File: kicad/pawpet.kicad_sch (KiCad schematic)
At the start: 35 parts, among them J1 USB4105-GF-A, J2 Conn_ARM_JTAG_SWD_10, J3 MOLEX, Q1 DMG2301L, U1 ATSAMD21G18A-A, U3 MX25R1635FM1IL0, Y1 32,768

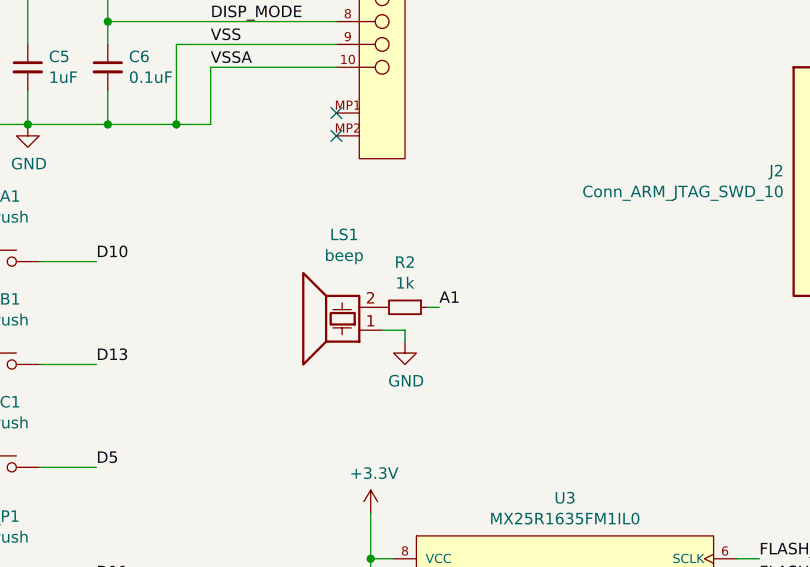
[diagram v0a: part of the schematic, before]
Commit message: updated to use latest adafruit samd base and gclk output to display vcom
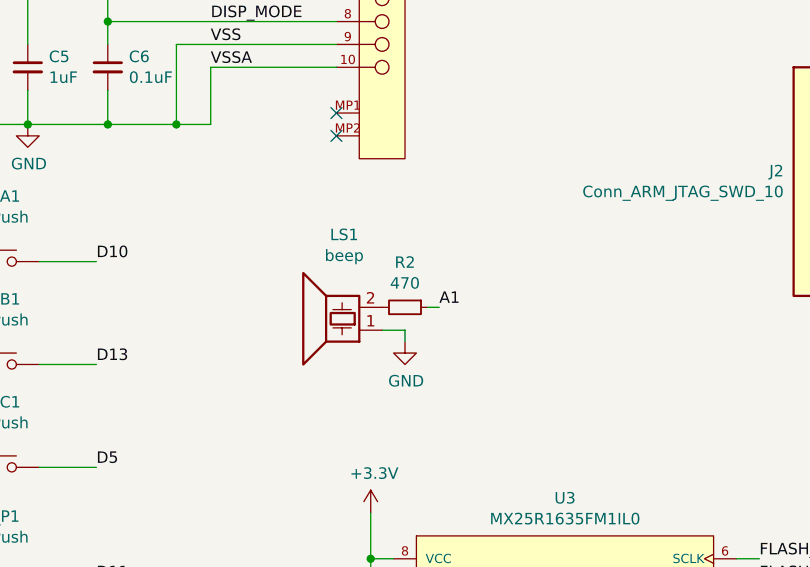
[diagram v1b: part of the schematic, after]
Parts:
- J2: footprint pawpet:ARM_JTAG -> Connector:Tag-Connect_TC2030-IDC-NL_2x03_P1.27mm_Vertical
- R2: value 1k -> 470
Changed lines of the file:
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@@
     (in_bom yes) (on_board yes)
     (property "Reference" "R2" (id 0) (at 87.63 115.6716 90))
-    (property "Value" "1k" (id 1) (at 87.63 117.983 90))
+    (property "Value" "470" (id 1) (at 87.63 117.983 90))
     (property "Footprint" "Resistor_SMD:R_0805_2012Metric" (id 2) (at 87.63 120.65 0)
       (effects (font (size 1.27 1.27)) hide)
@@
       (effects (font (size 1.27 1.27)) (justify right))
     )
-    (property "Footprint" "pawpet:ARM_JTAG" (id 2) (at 140.97 106.68 0)
+    (property "Footprint" "Connector:Tag-Connect_TC2030-IDC-NL_2x03_P1.27mm_Vertical" (id 2) (at 140.97 106.68 0)
       (effects (font (size 1.27 1.27)) hide)
     )
@@
     )
     (path "/00000000-0000-0000-0000-00005f61e5f9"
-      (reference "J2") (unit 1) (value "Conn_ARM_JTAG_SWD_10") (footprint "pawpet:ARM_JTAG")
+      (reference "J2") (unit 1) (value "Conn_ARM_JTAG_SWD_10") (footprint "Connector:Tag-Connect_TC2030-IDC-NL_2x03_P1.27mm_Vertical")
     )
     (path "/00000000-0000-0000-0000-00005f37490d"
@@
     )
     (path "/00000000-0000-0000-0000-00005f60ffb8"
-      (reference "R2") (unit 1) (value "1k") (footprint "Resistor_SMD:R_0805_2012Metric")
+      (reference "R2") (unit 1) (value "470") (footprint "Resistor_SMD:R_0805_2012Metric")
     )
     (path "/00000000-0000-0000-0000-00005f9e88e7"

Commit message: update to latest schematic, pcb, and stl files
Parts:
- J3: footprint pawpet:Molex-52892-1033-Manufacturer_Recommended_handsolder -> molex:Molex-52892-1033-Manufacturer_Recommended
- U1: footprint pawpet:TQFP-48-1EP_7x7mm_P0.5mm_EP5x5mm_handsolder -> Package_QFP:TQFP-48-1EP_7x7mm_P0.5mm_EP5x5mm
- U3: footprint pawpet:Macronix-SOP-8-150MIL-0-0-MFG_handsolder -> Package_SO:SOIC-8_5.23x5.23mm_P1.27mm
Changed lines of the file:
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@@
     (property "Reference" "U1" (id 0) (at 226.06 152.1206 0))
     (property "Value" "ATSAMD21G18A-A" (id 1) (at 226.06 154.432 0))
-    (property "Footprint" "pawpet:TQFP-48-1EP_7x7mm_P0.5mm_EP5x5mm_handsolder" (id 2) (at 248.92 148.59 0)
+    (property "Footprint" "Package_QFP:TQFP-48-1EP_7x7mm_P0.5mm_EP5x5mm" (id 2) (at 248.92 148.59 0)
       (effects (font (size 1.27 1.27)) hide)
     )
@@
       (effects (font (size 1.27 1.27)) hide)
     )
-    (property "Footprint" "pawpet:Molex-52892-1033-Manufacturer_Recommended_handsolder" (id 2) (at 77.47 71.12 0)
+    (property "Footprint" "molex:Molex-52892-1033-Manufacturer_Recommended" (id 2) (at 77.47 71.12 0)
       (effects (font (size 1.27 1.27)) hide)
     )
@@
     (property "Reference" "U3" (id 0) (at 105.41 141.859 0))
     (property "Value" "MX25R1635FM1IL0" (id 1) (at 105.41 144.1704 0))
-    (property "Footprint" "pawpet:Macronix-SOP-8-150MIL-0-0-MFG_handsolder" (id 2) (at 83.82 163.83 0)
+    (property "Footprint" "Package_SO:SOIC-8_5.23x5.23mm_P1.27mm" (id 2) (at 83.82 163.83 0)
       (effects (font (size 1.27 1.27)) hide)
     )
@@
     )
     (path "/00000000-0000-0000-0000-00005f37490d"
-      (reference "J3") (unit 1) (value "MOLEX") (footprint "pawpet:Molex-52892-1033-Manufacturer_Recommended_handsolder")
+      (reference "J3") (unit 1) (value "MOLEX") (footprint "molex:Molex-52892-1033-Manufacturer_Recommended")
     )
     (path "/00000000-0000-0000-0000-00005f60398a"
@@
     )
     (path "/00000000-0000-0000-0000-00005f344907"
-      (reference "U1") (unit 1) (value "ATSAMD21G18A-A") (footprint "pawpet:TQFP-48-1EP_7x7mm_P0.5mm_EP5x5mm_handsolder")
+      (reference "U1") (unit 1) (value "ATSAMD21G18A-A") (footprint "Package_QFP:TQFP-48-1EP_7x7mm_P0.5mm_EP5x5mm")
     )
     (path "/00000000-0000-0000-0000-00005f4d7ef1"
-      (reference "U3") (unit 1) (value "MX25R1635FM1IL0") (footprint "pawpet:Macronix-SOP-8-150MIL-0-0-MFG_handsolder")
+      (reference "U3") (unit 1) (value "MX25R1635FM1IL0") (footprint "Package_SO:SOIC-8_5.23x5.23mm_P1.27mm")
     )
     (path "/00000000-0000-0000-0000-00005f365140"
